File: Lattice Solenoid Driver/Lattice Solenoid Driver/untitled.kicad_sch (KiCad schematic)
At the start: 9 parts, among them U20 DRV8825PWPR

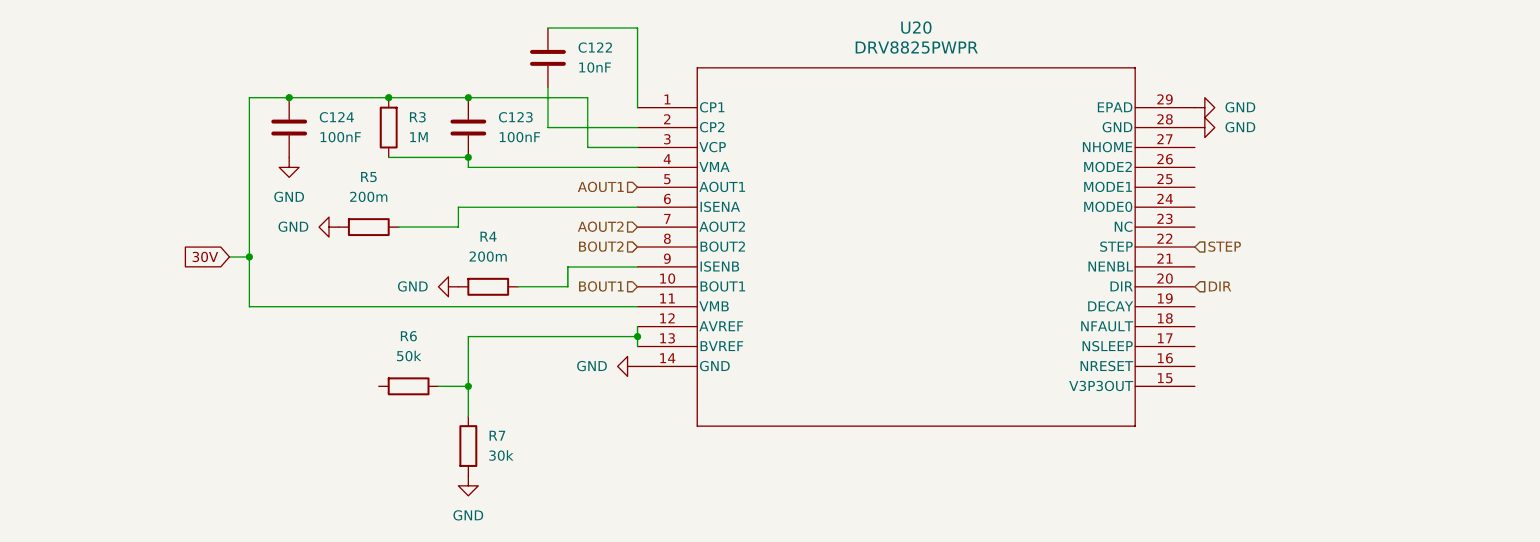
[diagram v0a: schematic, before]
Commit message: added stepper sch
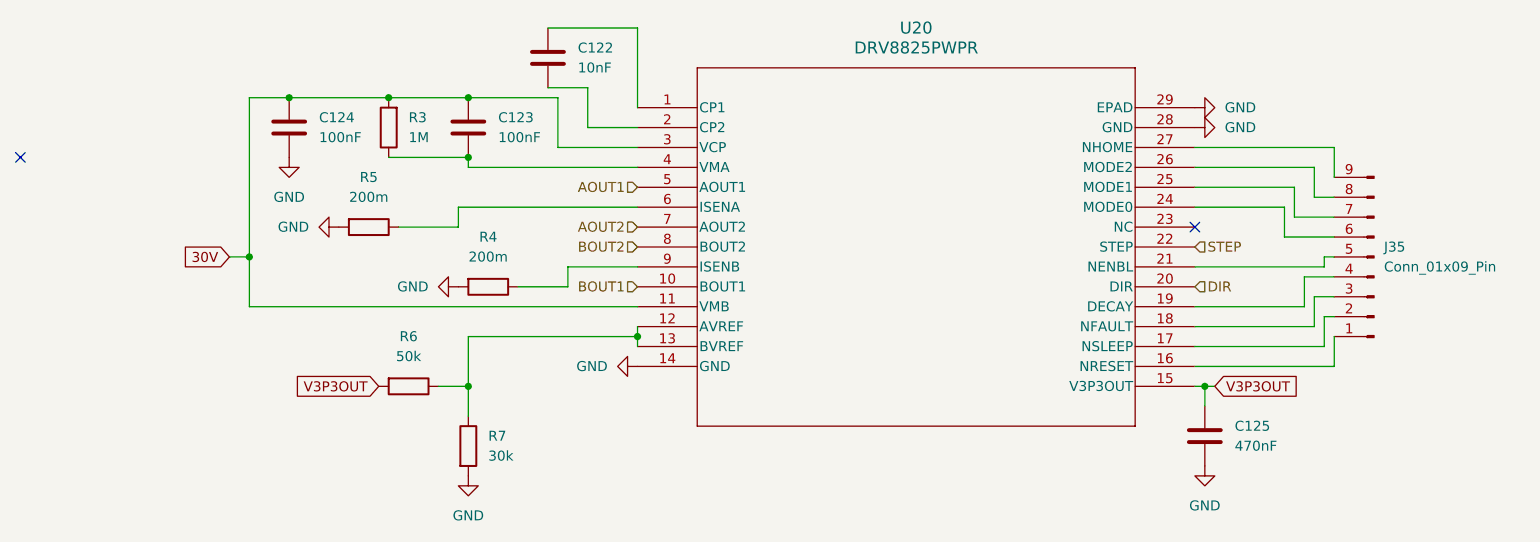
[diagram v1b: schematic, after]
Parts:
- added C125: 470nF, Capacitor_SMD:C_0805_2012Metric, symbol Device:C
- added J35: Conn_01x09_Pin, Connector_PinHeader_2.54mm:PinHeader_1x09_P2.54mm_Vertical, symbol Connector:Conn_01x09_Pin
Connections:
- net GND: now also C125.2
- net V3P3OUT: now reaches U20.15 (V3P3OUT)
- net V3P3OUT: now also R6.2, C125.1
- net at U20.16 (NRESET): now also J35.1 (Pin_1)
- net at U20.17 (NSLEEP): now also J35.2 (Pin_2)
- net at U20.18 (NFAULT): now also J35.3 (Pin_3)
- net at U20.19 (DECAY): now also J35.4 (Pin_4)
- net at U20.21 (NENBL): now also J35.5 (Pin_5)
- net at U20.24 (MODE0): now also J35.6 (Pin_6)
- net at U20.25 (MODE1): now also J35.7 (Pin_7)
- net at U20.26 (MODE2): now also J35.8 (Pin_8)
- net at U20.27 (NHOME): now also J35.9 (Pin_9)
- no-connect marks 0 -> 2

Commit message: grbrs
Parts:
- U20: Part # (none) -> C81582
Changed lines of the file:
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@@
+			)
+		)
+		(property "Part #" "C81582"
+			(at 107.95 86.36 0)
+			(effects
+				(font
+					(size 1.27 1.27)
+				)
 			)
 		)
